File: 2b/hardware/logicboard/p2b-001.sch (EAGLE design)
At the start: 77 parts, among them IC1 74LS06N, IC2 4066N, J1 MKR, J10 1-Wire, J2 GPIO, J20 GPIO, J3 Vcc, J4** RLY2, J5 SPI, J6 LED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

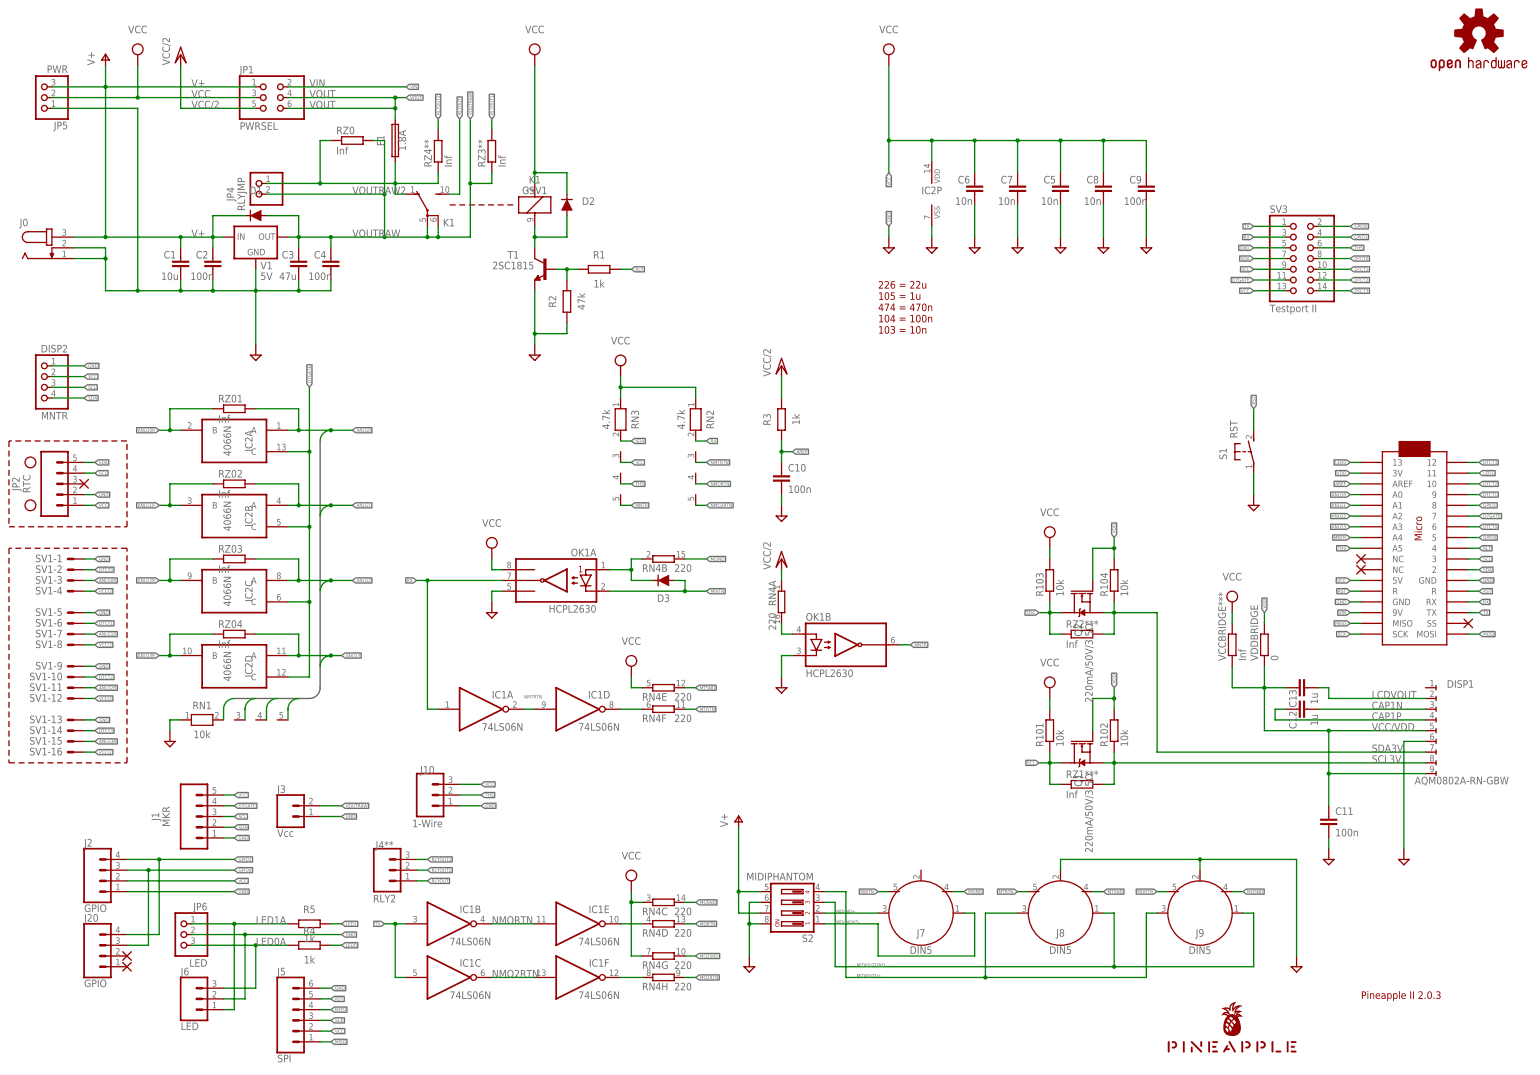
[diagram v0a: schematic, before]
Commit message: vdd/vcc xbar for lcd monitor.
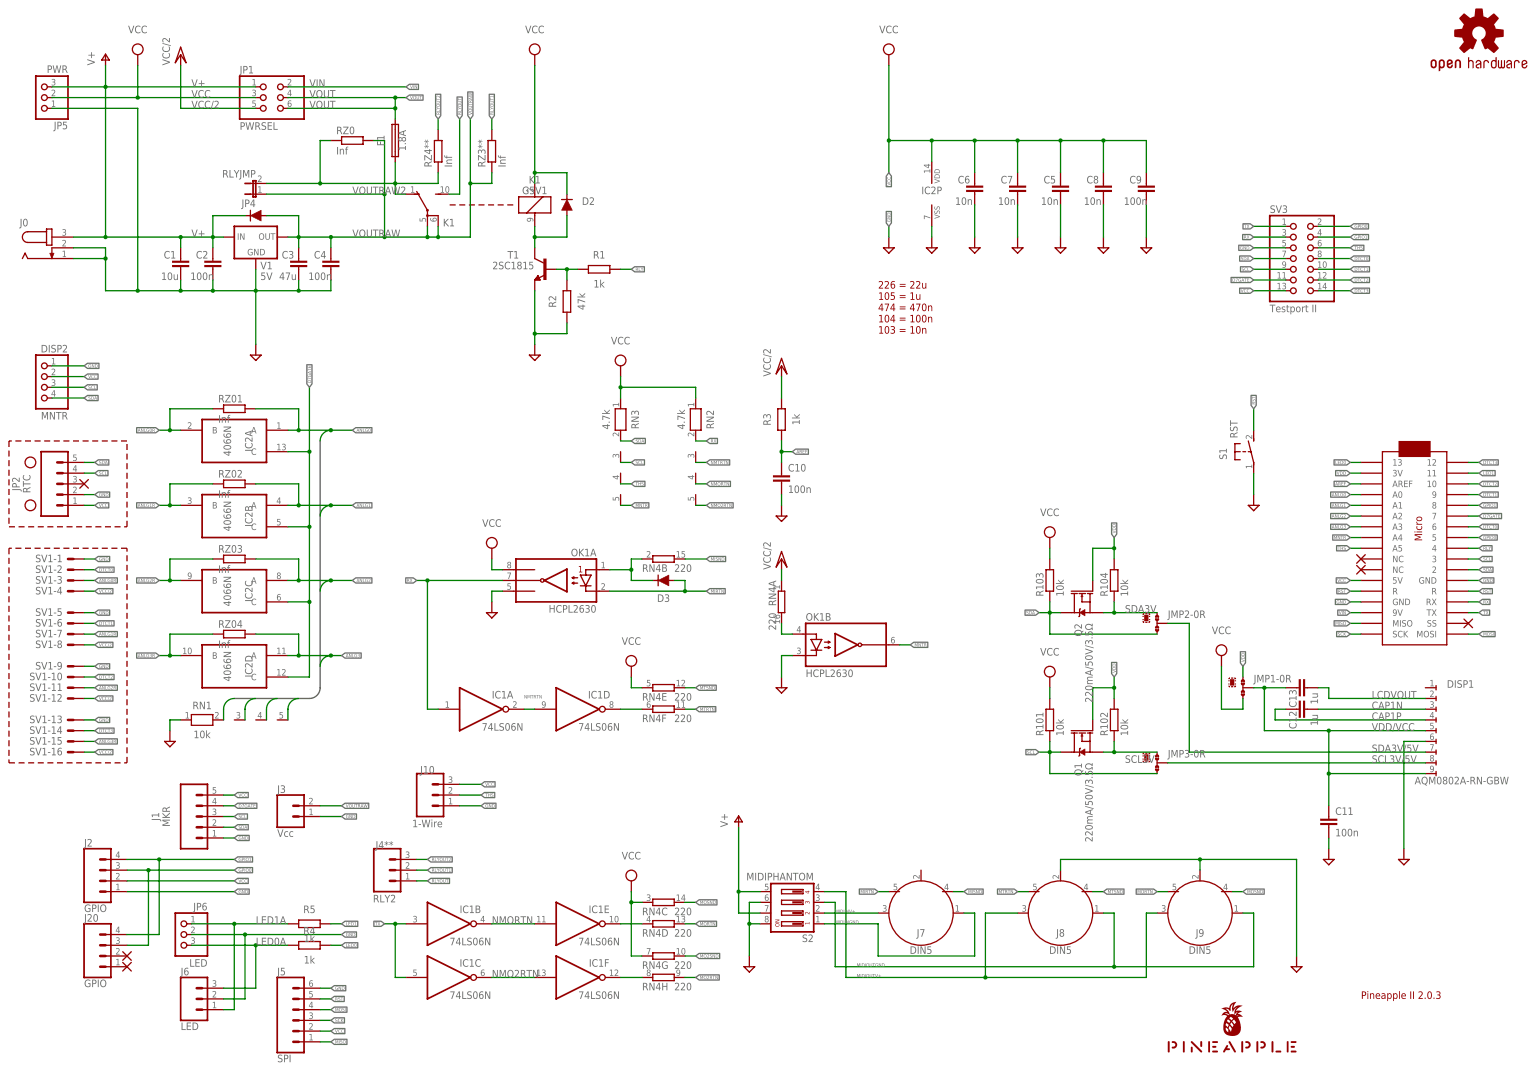
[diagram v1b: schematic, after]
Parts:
- removed RZ1***, RZ2***, VCCBRIDGE***: Inf, rcl:R-EU_M2012
- removed VDDBRIDGE: 0, rcl:R-EU_M2012
- added JMP1, JMP2, JMP3: 0R-JUMPA, jump-0r-smd:0R-JUMPA
- JP4: device pinhead:PINHD-1X2 -> jumper:JP1E
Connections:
- removed net VCC/VDD: C11.1, C13.1, DISP1.5, DISP1.9, VCCBRIDGE***.1, VDDBRIDGE.1
- new net SCL3V/5V: DISP1.8, JMP3-0R.2
- new net SDA3V/5V: DISP1.7, JMP2-0R.2
- new net VDD/VCC: C11.1, C13.1, DISP1.5, DISP1.9, JMP1-0R.2
- net SCL: now also JMP3-0R.3; no longer RZ1***.1
- net SCL3V: now also JMP3-0R.1; no longer DISP1.8, RZ1***.2
- net SDA: now also JMP2-0R.3; no longer RZ2***.1
- net SDA3V: now also JMP2-0R.1; no longer DISP1.7, RZ2***.2
- net VCC: now also JMP1-0R.3; no longer VCCBRIDGE***.2
- net VDD: now also JMP1-0R.1; no longer VDDBRIDGE.2
- net VOUTRAW: now also JP4.1; no longer JP4.2
- net VOUTRAW2: now also JP4.2; no longer JP4.1
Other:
- moved on the sheet: Q1, R101, R102
